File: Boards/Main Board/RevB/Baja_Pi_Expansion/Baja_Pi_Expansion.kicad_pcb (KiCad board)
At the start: 4 copper layers, 85 x 56 mm, 25 parts, among them J1 Conn_02x10_Counter_Clockwise, J2 Conn_02x12_Counter_Clockwise, J3 Screw_Terminal_01x04, J4 Conn_02x20_Odd_Even, J5 Conn_01x03_Male, J6 Screw_Terminal_01x07, U1 HDSP-7403

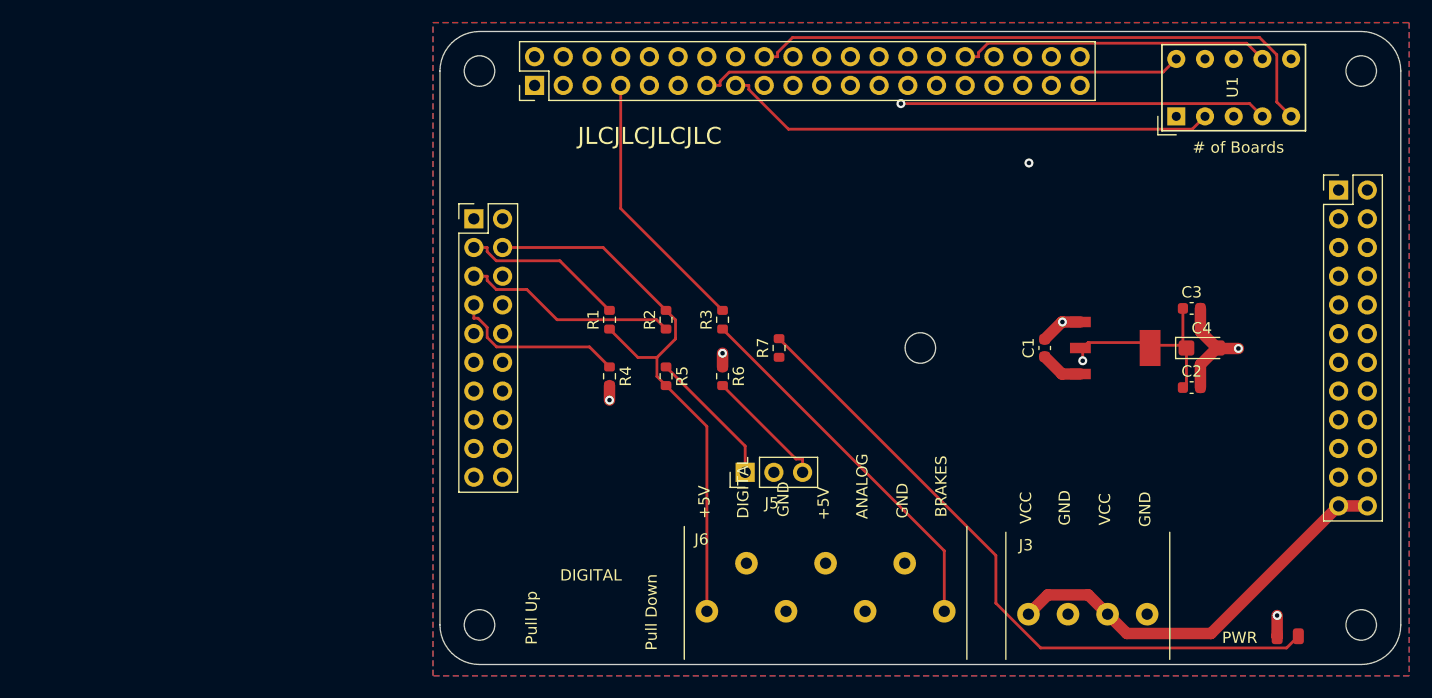
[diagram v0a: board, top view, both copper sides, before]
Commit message: Removed footprints from PCB on Main-RevB
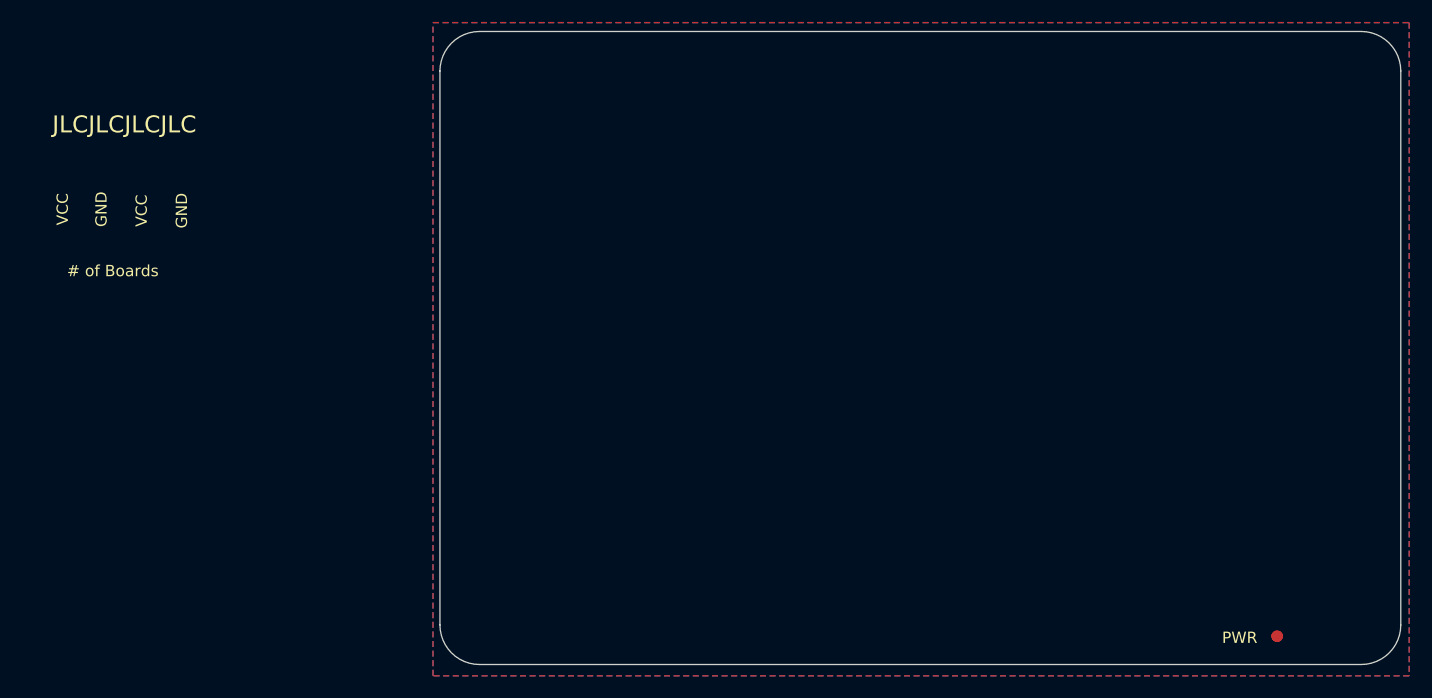
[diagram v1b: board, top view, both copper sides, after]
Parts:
- removed C1: 0.1uF, Capacitor_SMD:C_0603_1608Metric
- removed C2: 1uF, Capacitor_SMD:C_0603_1608Metric
- removed C3: 1uF_cpu, Capacitor_SMD:C_0603_1608Metric
- removed C4: 4.7uF_16V_cpu, Capacitor_Tantalum_SMD:CP_EIA-3216-18_Kemet-A
- removed D1: LED, Custom Footprints:LED_0805_2012Metric
- removed H1: MH1, MountingHole:MountingHole_2.7mm_M2.5
- removed H2: MH2, MountingHole:MountingHole_2.7mm_M2.5
- removed H3: MH3, MountingHole:MountingHole_2.7mm_M2.5
- removed H4: MH4, MountingHole:MountingHole_2.7mm_M2.5
- removed H5: MH_c, MountingHole:MountingHole_2.7mm_M2.5
- removed J1: Conn_02x10_Counter_Clockwise, Connector_PinHeader_2.54mm:PinHeader_2x10_P2.54mm_Vertical
- removed J2: Conn_02x12_Counter_Clockwise, Connector_PinHeader_2.54mm:PinHeader_2x12_P2.54mm_Vertical
- removed J3: Screw_Terminal_01x04, Custom Footprints:Spring_4
- removed J4: Conn_02x20_Odd_Even, Connector_PinHeader_2.54mm:PinHeader_2x20_P2.54mm_Vertical
- removed J5: Conn_01x03_Male, Connector_PinHeader_2.54mm:PinHeader_1x03_P2.54mm_Vertical
- removed J6: Screw_Terminal_01x07, Custom Footprints:Spring_7
- removed R1, R2: 4.7k, Resistor_SMD:R_0603_1608Metric
- removed R3, R4, R5, R6: R_US, Resistor_SMD:R_0603_1608Metric
- removed R7: 350?, Resistor_SMD:R_0603_1608Metric
- removed U1: HDSP-7403, Display_7Segment:HDSP-7401
- removed VR1: LM1117IMPX-5.0, LM1117IMPX-5:SOT230P700X180-4N
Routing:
- net /5v: track 133.1 -> 0.00 mm, vias 1 -> 0
- net /analog_in: track 110.0 -> 0.00 mm
- net /dig_in: track 105.5 -> 0.00 mm
- net /gpio8: track 97.5 -> 0.00 mm
- net /gpio7: track 90.9 -> 0.00 mm, vias 1 -> 0
- net /gpio6: track 83.7 -> 0.00 mm
- net /gpio11: track 79.5 -> 0.00 mm
- net /gpio1: track 64.6 -> 0.00 mm
- net /miso: track 64.2 -> 0.00 mm
- net /reset: track 62.7 -> 0.00 mm
- net /miso2_pwm: track 61.0 -> 0.00 mm
- net Net-(D1-Pad2): track 60.2 -> 0.00 mm
- net /gpio4: track 57.6 -> 0.00 mm
- net /3v3: track 57.5 -> 0.00 mm
- net /gpio9: track 55.6 -> 0.00 mm
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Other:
- board text added: "RIT Baja SDAQ Main Board Revision B Adam Seidman (732) 882-9717"
- board text removed: "+5V"
- board text removed: "ANALOG"
- board text removed: "BRAKES"
- board text removed: "DIGITAL"
- board text removed: "Pull Down"
- board text removed: "Pull Up"
- board text removed: "RIT Baja SDAQ Main Board Revision A Adam Seidman (732) 882-9717"

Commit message: Turned Main-RevB from 4 layers into 2
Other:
- copper layers 4 -> 2
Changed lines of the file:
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@@
   (layers
     (0 F.Cu signal)
-    (1 In1.Cu signal)
-    (2 In2.Cu signal)
     (31 B.Cu signal)
     (32 B.Adhes user)

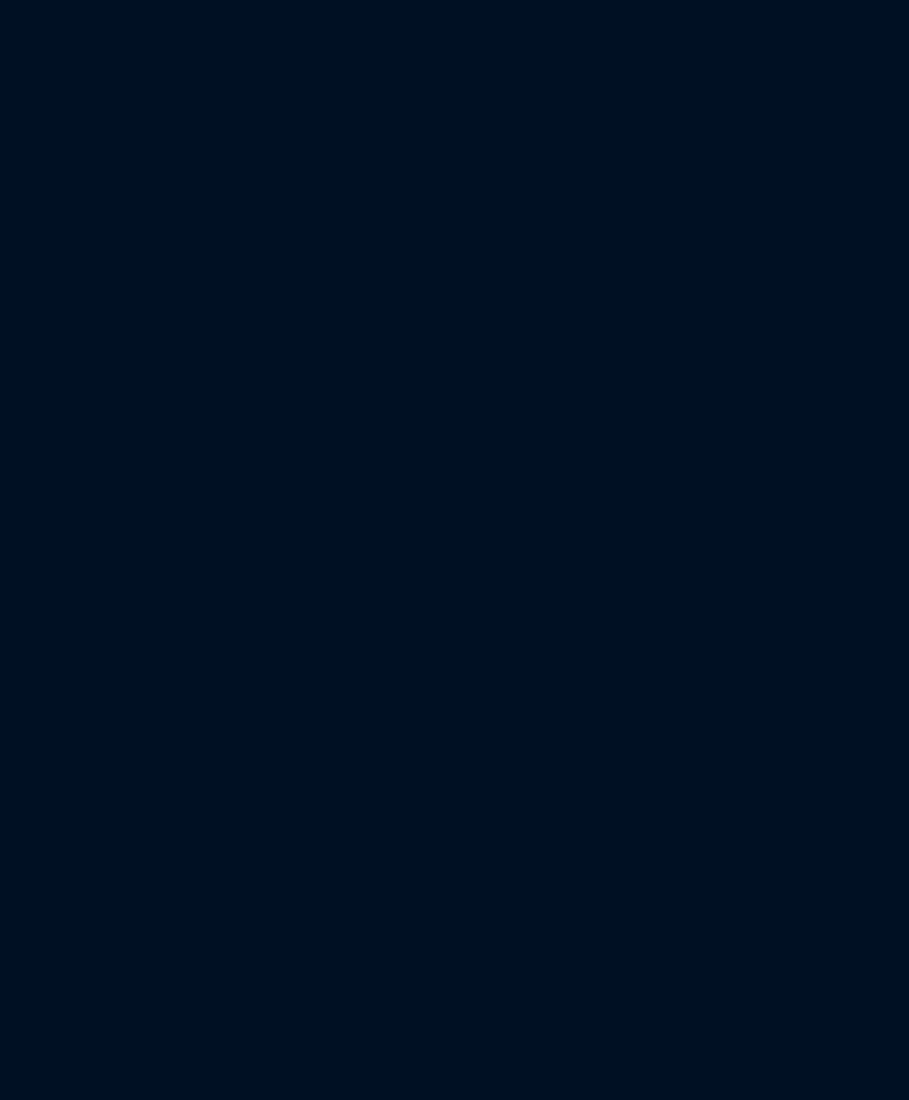
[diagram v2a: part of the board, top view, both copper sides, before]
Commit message: Added Footprints and .net to Main-RevB
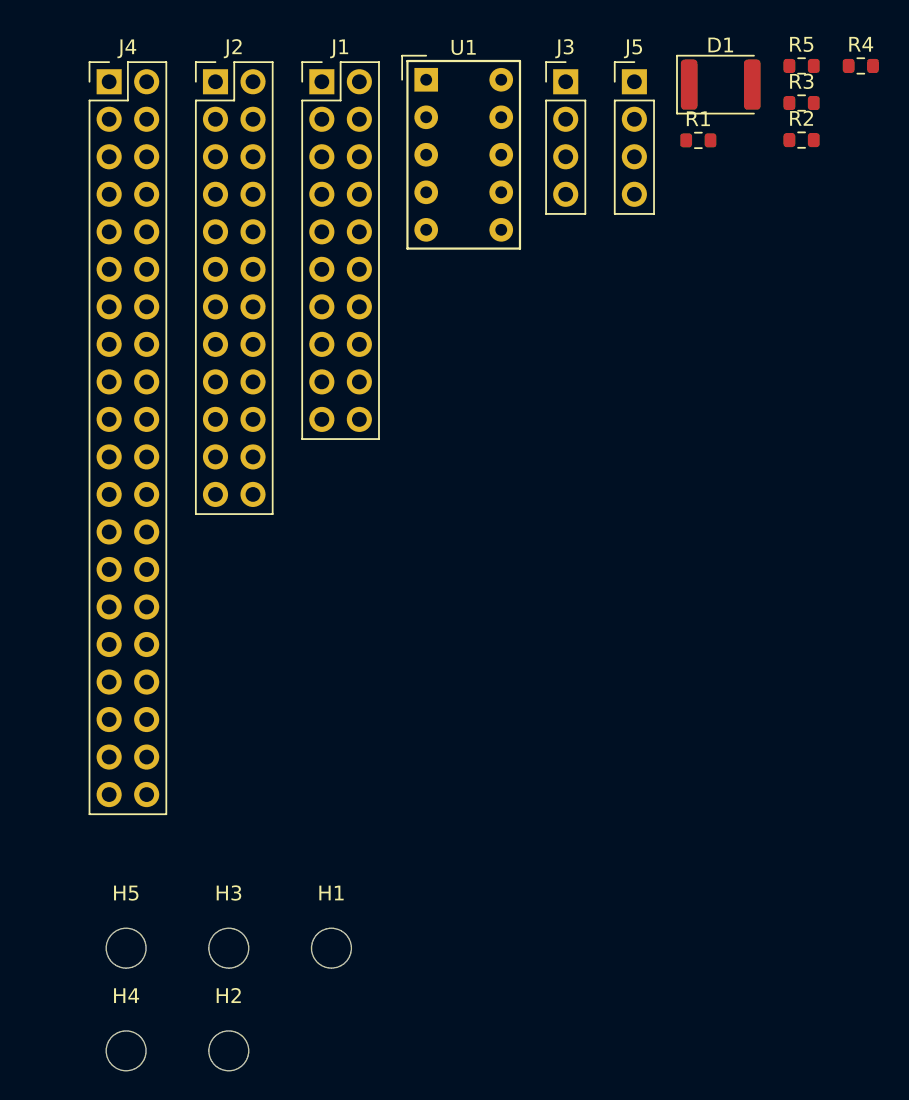
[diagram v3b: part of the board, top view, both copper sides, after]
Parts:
- added D1: LED, LED_SMD:LED_1812_4532Metric, F.Cu at (307.6, 66.2)
- added H1: MH1, MountingHole:MountingHole_2.7mm_M2.5, F.Cu at (281.3, 124.6)
- added H2: MH2, MountingHole:MountingHole_2.7mm_M2.5, F.Cu at (274.3, 131.6)
- added H3: MH3, MountingHole:MountingHole_2.7mm_M2.5, F.Cu at (274.3, 124.6)
- added H4: MH4, MountingHole:MountingHole_2.7mm_M2.5, F.Cu at (267.4, 131.6)
- added H5: MH_c, MountingHole:MountingHole_2.7mm_M2.5, F.Cu at (267.4, 124.6)
- added J1: Conn_02x10_Counter_Clockwise, Connector_PinHeader_2.54mm:PinHeader_2x10_P2.54mm_Vertical, F.Cu at (280.6, 66.0)
- added J2: Conn_02x12_Counter_Clockwise, Connector_PinHeader_2.54mm:PinHeader_2x12_P2.54mm_Vertical, F.Cu at (273.4, 66.0)
- added J3: Screw_Terminal_01x04, Connector_PinHeader_2.54mm:PinHeader_1x04_P2.54mm_Vertical, F.Cu at (297.1, 66.0)
- added J4: Conn_02x20_Odd_Even, Connector_PinHeader_2.54mm:PinHeader_2x20_P2.54mm_Vertical, F.Cu at (266.2, 66.0)
- added J5: Screw_Terminal_01x04, Connector_PinHeader_2.54mm:PinHeader_1x04_P2.54mm_Vertical, F.Cu at (301.8, 66.0)
- added R1: 4.7k, Resistor_SMD:R_0603_1608Metric, F.Cu at (306.1, 69.9)
- added R2: 4.7k, Resistor_SMD:R_0603_1608Metric, F.Cu at (313.1, 69.9)
- added R3: R_US, Resistor_SMD:R_0603_1608Metric, F.Cu at (313.1, 67.4)
- added R4: R_US, Resistor_SMD:R_0603_1608Metric, F.Cu at (317.1, 64.9)
- added R5: 350?, Resistor_SMD:R_0603_1608Metric, F.Cu at (313.1, 64.9)
- added U1: HDSP-7403, Display_7Segment:HDSP-7401, F.Cu at (287.7, 65.8)

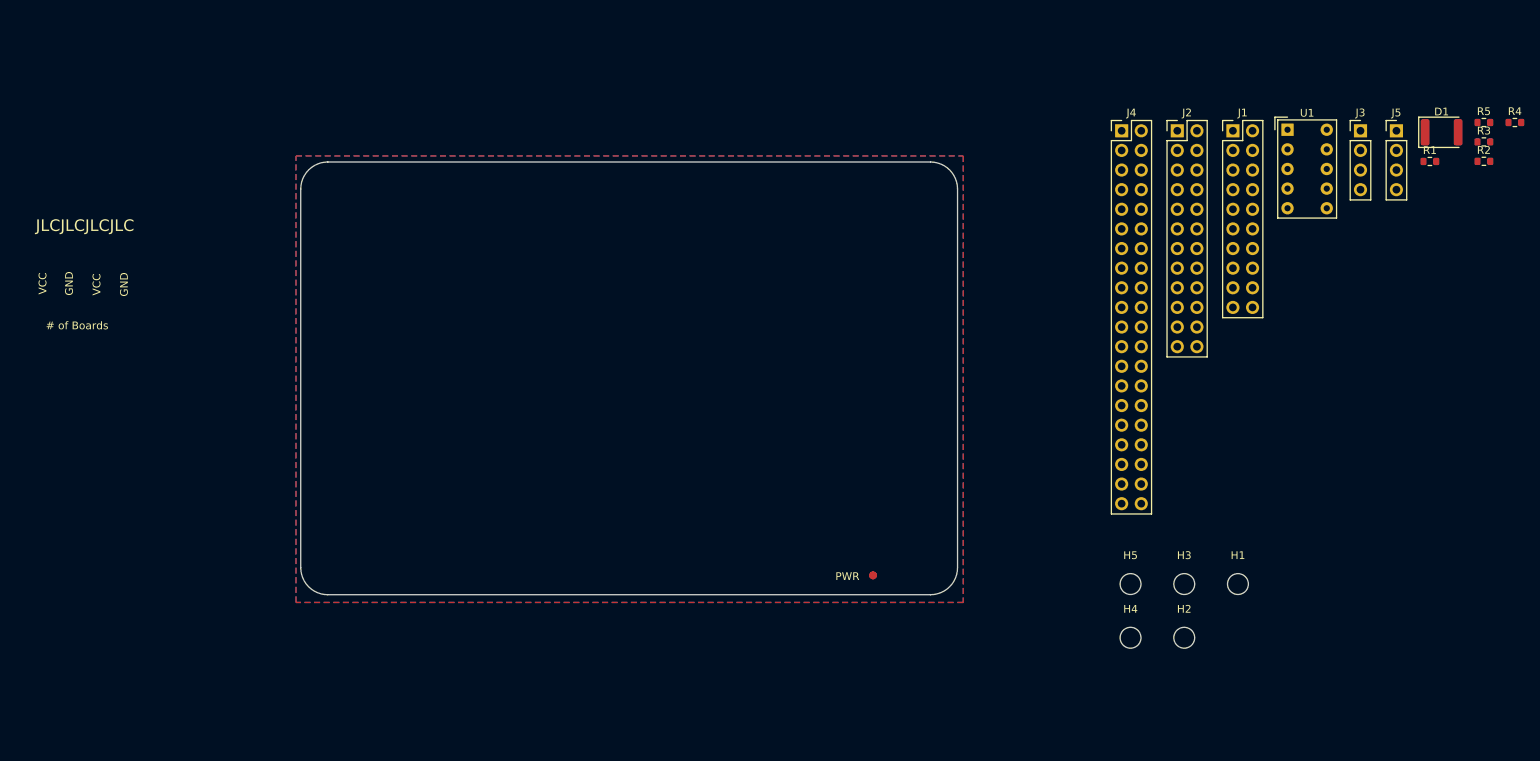
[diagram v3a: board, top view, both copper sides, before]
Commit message: Begin to put components in place on Main-RevB
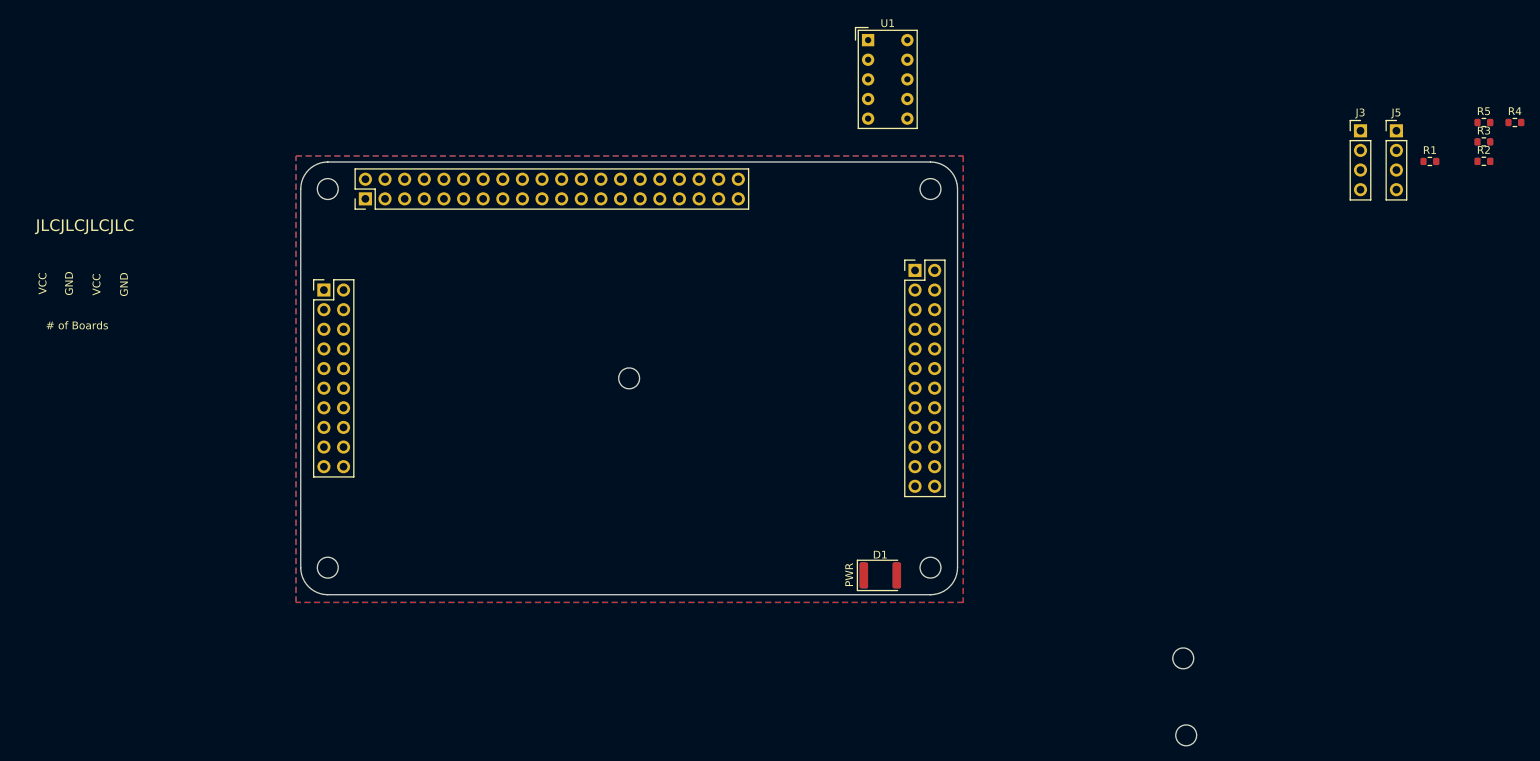
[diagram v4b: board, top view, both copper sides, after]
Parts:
- added H6: MH4, MountingHole:MountingHole_2.7mm_M2.5, F.Cu at (163.5, 73.5)
- added H7: MH_c, MountingHole:MountingHole_2.7mm_M2.5, F.Cu at (274.6, 144.2)
- moved J1 119.4 mm to (163.0, 86.6)
- moved H4 104.3 mm to (163.5, 122.5)
- moved J4 98.3 mm to (168.4, 74.8), turned to 90 degrees
- moved D1 92.6 mm to (235.0, 123.5)
- moved H1 83.2 mm to (202.5, 98.0)
- moved H5 57.3 mm to (241.5, 73.5)
- moved U1 55.5 mm to (233.4, 54.2)
- moved J2 38.4 mm to (239.5, 84.0)
- moved H3 32.9 mm to (241.5, 122.5)
- moved H2 2.67 mm to (274.2, 134.2)
